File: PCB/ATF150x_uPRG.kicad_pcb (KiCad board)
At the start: 2 copper layers, 38.1 x 22.9 mm, 23 parts, among them J1 Adafruit_2264, J2 Altera JTAG-A+VPP, U2 MAX662A

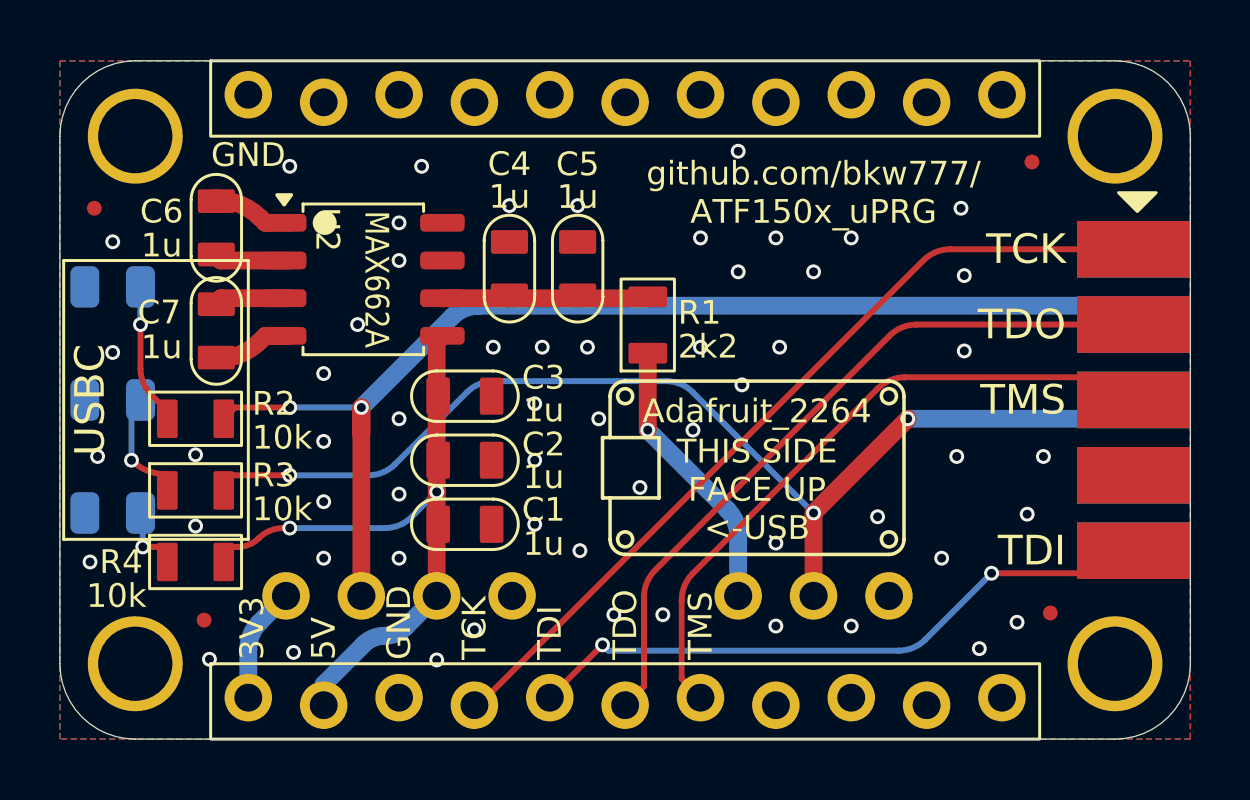
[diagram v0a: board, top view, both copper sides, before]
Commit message: silkscreen & minor trace move
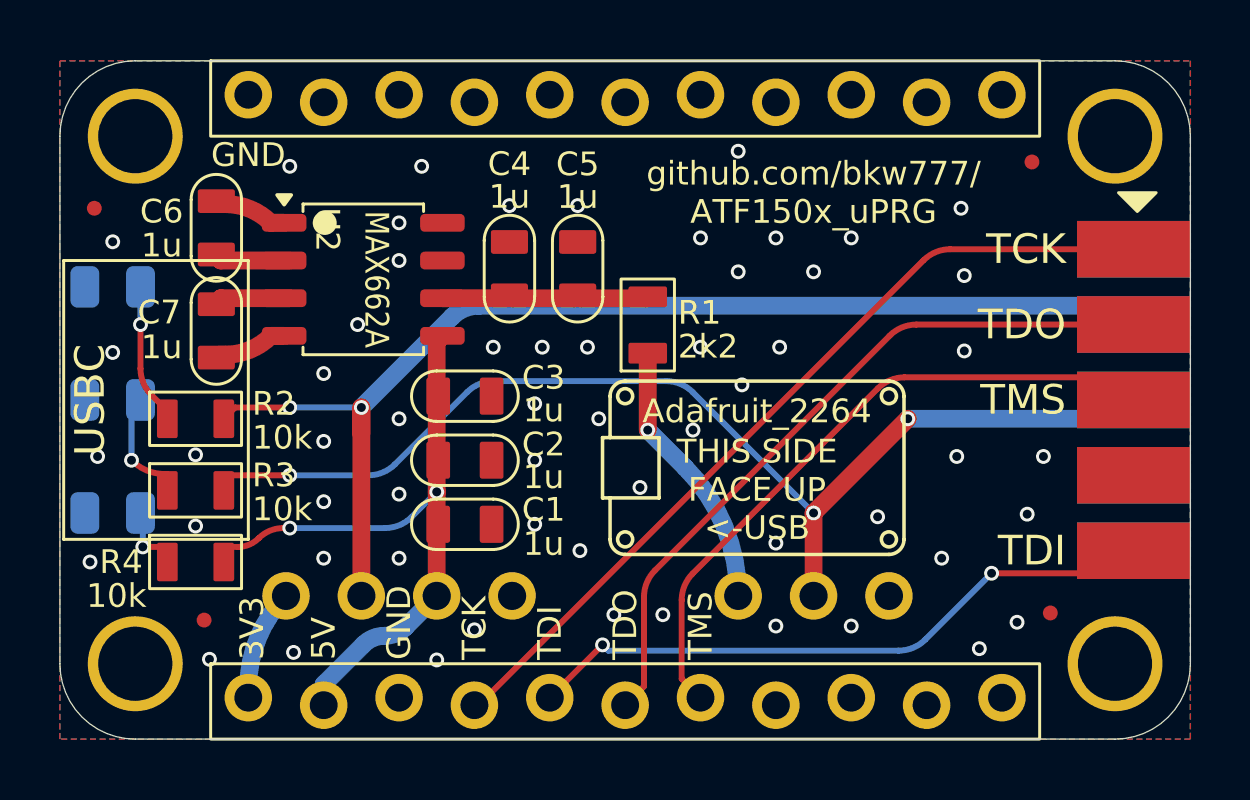
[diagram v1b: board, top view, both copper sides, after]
